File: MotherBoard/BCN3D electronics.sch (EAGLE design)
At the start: 195 parts, among them IC1 LM358D, IC2 FT232RL, IC3 LM311D, K1 G5L, Q1 MOSFET-NSOIC8, Q2 MOSFET-NSOIC8, Q3 MOSFET-NSOIC8, Q4 MMBT2222A, Q5 MMBT2222A, Q9 MMBT2222A, U1 INA169, X0 FFC_15V_90G_1MM, X1 FFC_15V_90G_1MM, Y0 FFC_15V_90G_1MM

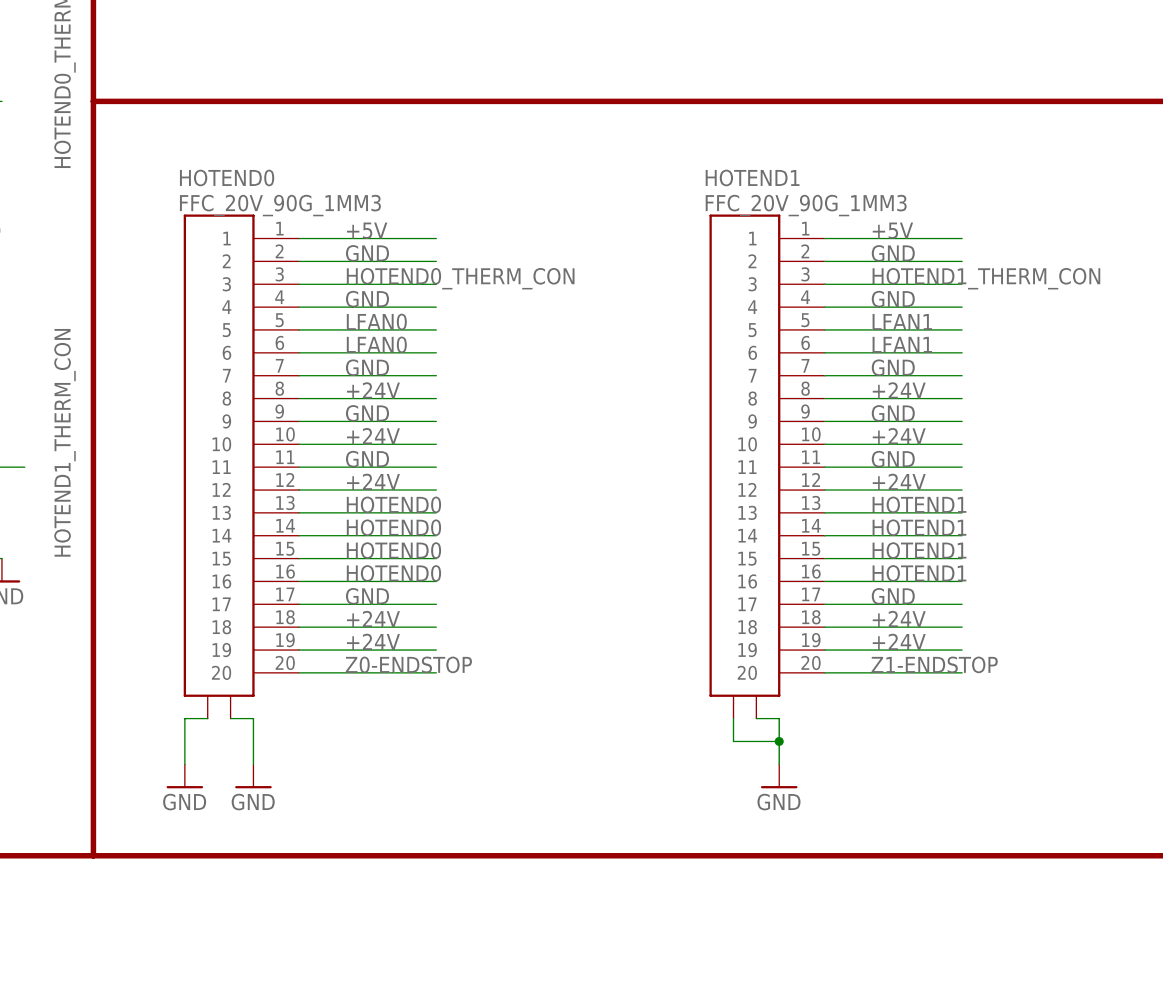
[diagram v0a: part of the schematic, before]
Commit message: Motherboard updated to new version REV.G
Basically the only change in REV.G is the 20 contacts Flat Flexible
Cable connector.
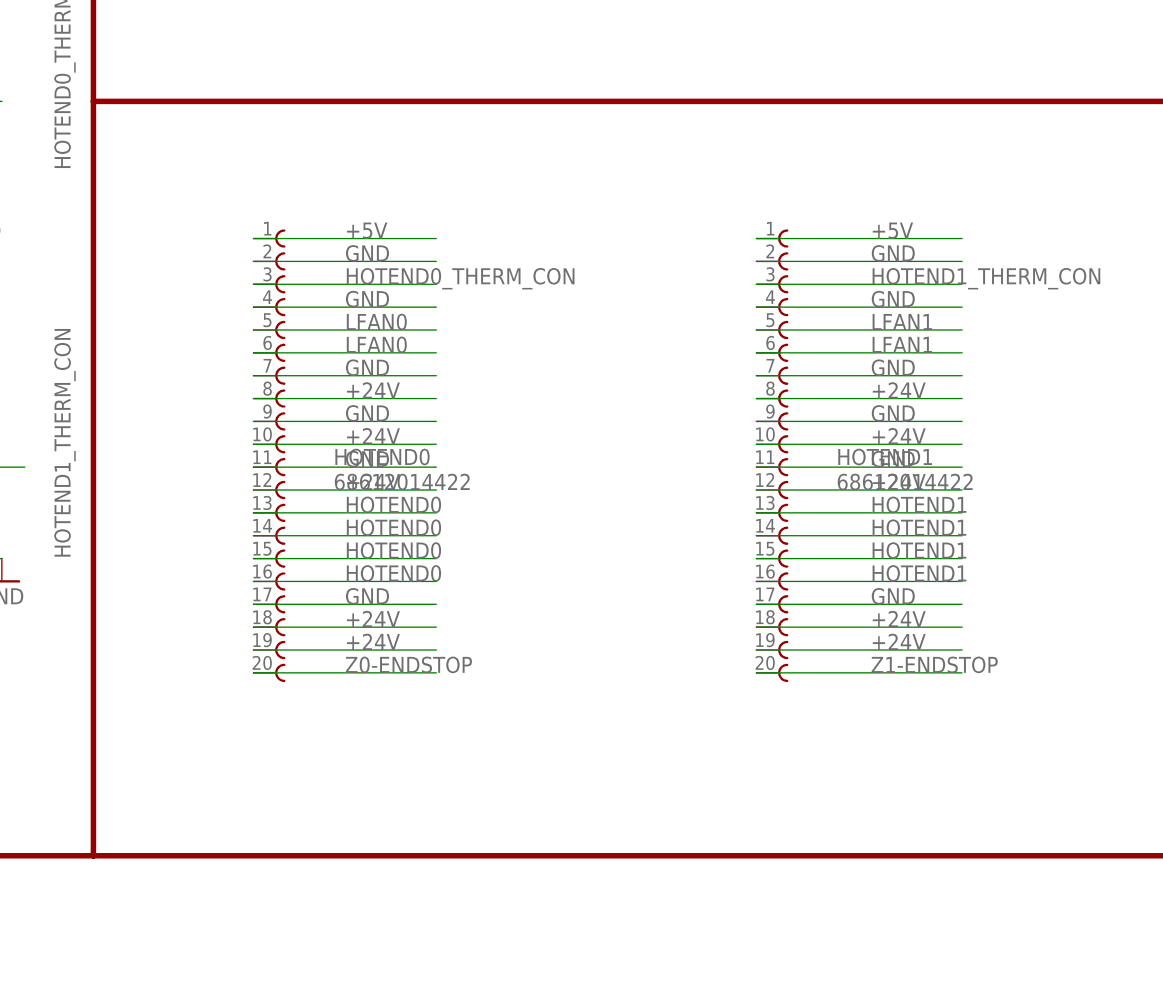
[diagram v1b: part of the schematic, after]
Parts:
- HOTEND0, HOTEND1: value FFC_20V_90G_1MM3 -> 68612014422; device MarcEagleParts:FFC_20V_90G_1MM3 -> FPC_FFC_Connectors_:68612014422
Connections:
- net GND: no longer HOTEND0.GND@1, HOTEND0.GND@2, HOTEND1.GND@1, HOTEND1.GND@2
